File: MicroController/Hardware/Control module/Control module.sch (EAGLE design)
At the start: 53 parts, among them J1 1X2-3.5MM, J2 RJ45-TRAFO, J3 RJ45-TRAFO, J4 RJ45-TRAFO, Q1 BSS138, Q2 BSS138, Q3 BSS138, Q4 BSS138, Q5 BSS138, Q6 BSS138, Q7 BSS138, Q8 BSS138, U1 CD74HC4067SM96, U3 TLV1117-33CDCY

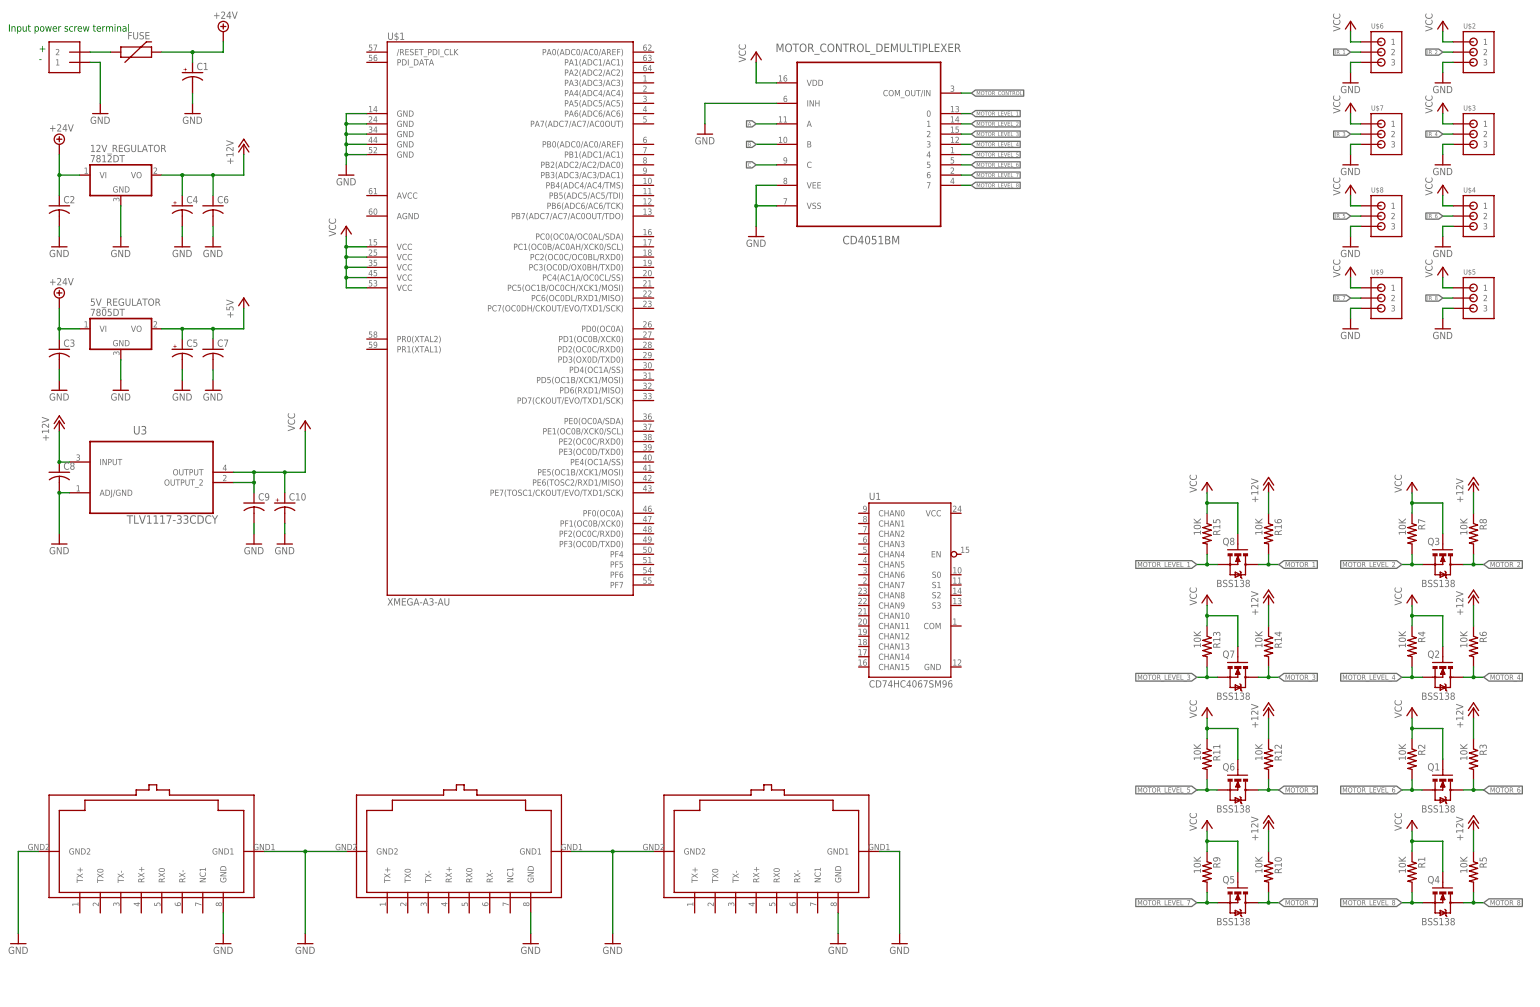
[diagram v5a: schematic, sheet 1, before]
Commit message: Looked into motor drivers and changed some components
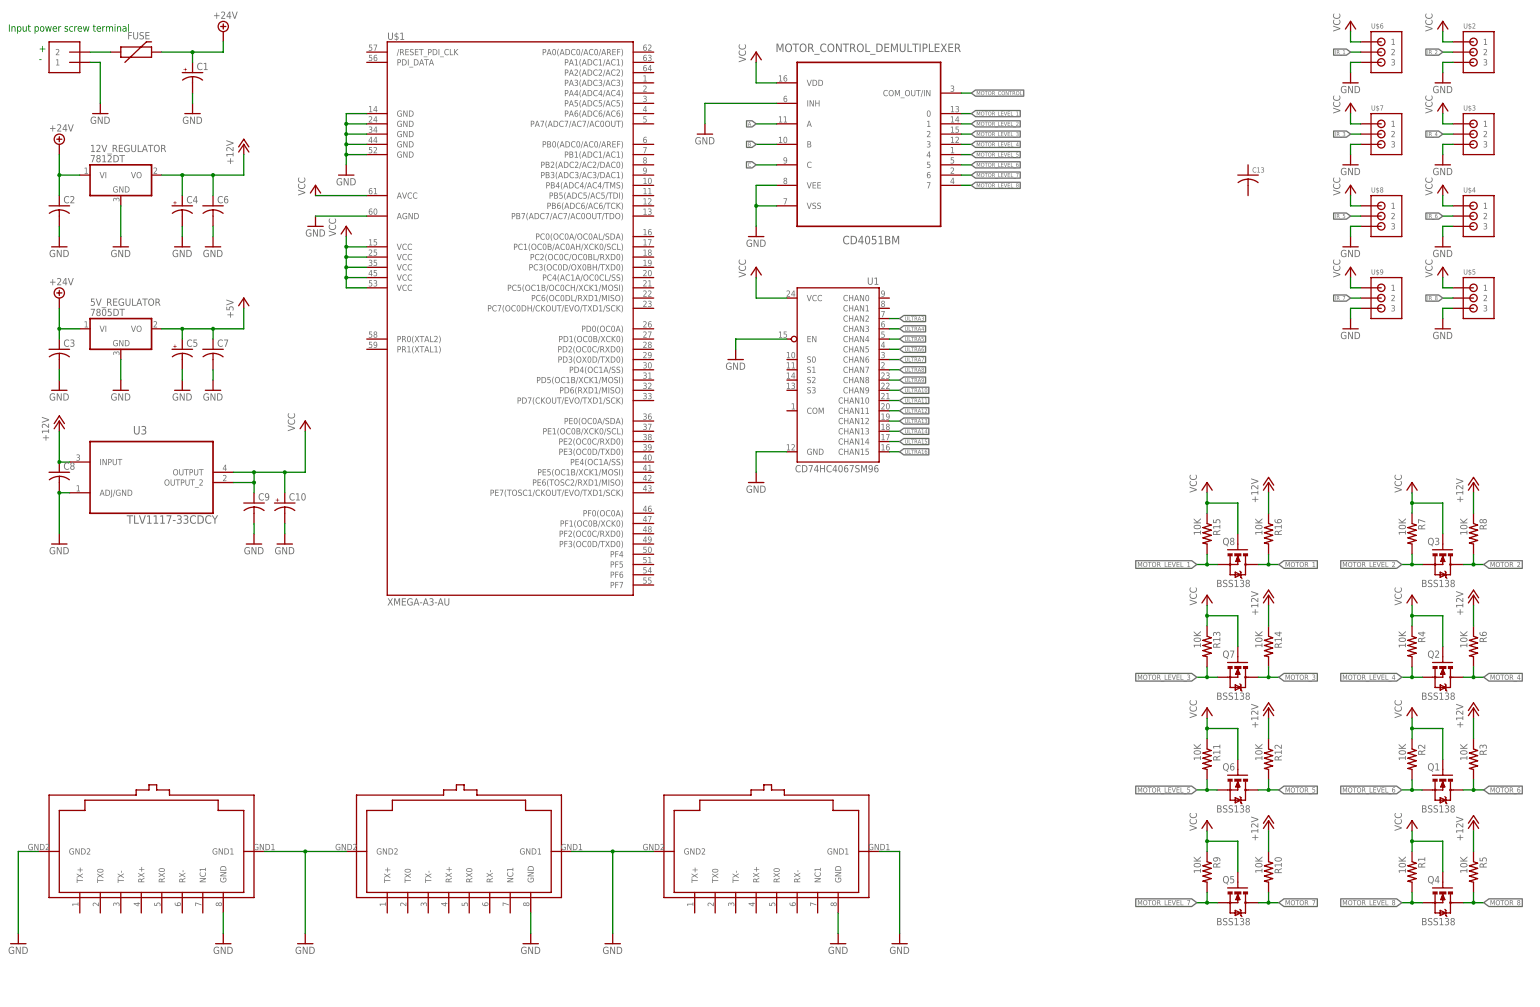
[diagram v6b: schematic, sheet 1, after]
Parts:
- added C13: (no value), adafruit:C-USC0805
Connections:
- new net ULTRA10: U1.CHAN9
- new net ULTRA11: U1.CHAN10
- new net ULTRA12: U1.CHAN11
- new net ULTRA13: U1.CHAN12
- new net ULTRA14: U1.CHAN13
- new net ULTRA15: U1.CHAN14
- new net ULTRA16: U1.CHAN15
- new net ULTRA3: U1.CHAN2
- new net ULTRA4: U1.CHAN3
- new net ULTRA5: U1.CHAN4
- new net ULTRA6: U1.CHAN5
- new net ULTRA7: U1.CHAN6
- new net ULTRA8: U1.CHAN7
- new net ULTRA9: U1.CHAN8
- net GND: now also U$1.AGND, U1.EN, U1.GND
- net VCC: now also U$1.AVCC, U1.VCC
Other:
- moved on the sheet: U1
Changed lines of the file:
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@@
 <part name="P+29" library="supply1" library_urn="urn:adsk.eagle:library:371" deviceset="VCC" device=""/>
 <part name="P+30" library="supply1" library_urn="urn:adsk.eagle:library:371" deviceset="VCC" device=""/>
+<part name="P+31" library="supply1" library_urn="urn:adsk.eagle:library:371" deviceset="VCC" device=""/>
+<part name="GND32" library="supply1" library_urn="urn:adsk.eagle:library:371" deviceset="GND" device=""/>
+<part name="GND33" library="supply1" library_urn="urn:adsk.eagle:library:371" deviceset="GND" device=""/>
+<part name="GND34" library="supply1" library_urn="urn:adsk.eagle:library:371" deviceset="GND" device=""/>
+<part name="P+32" library="supply1" library_urn="urn:adsk.eagle:library:371" deviceset="VCC" device=""/>
+<part name="C13" library="adafruit" library_urn="urn:adsk.eagle:library:420" deviceset="C-US" device="C0805"/>
 </parts>
 <sheets>
@@
 </plain>
 <instances>
-<instance part="U1" gate="U1" x="213.36" y="68.58"/>
+<instance part="U1" gate="U1" x="195.58" y="121.92" rot="MR0"/>
 <instance part="U$1" gate="G$1" x="114.3" y="134.62"/>
 <instance part="MOTOR_CONTROL_DEMULTIPLEXER" gate="A" x="203.2" y="180.34" smashed="yes">
@@
 <instance part="P+29" gate="VCC" x="345.44" y="147.32"/>
 <instance part="P+30" gate="VCC" x="322.58" y="147.32"/>
+<instance part="P+31" gate="VCC" x="66.04" y="167.64"/>
+<instance part="GND32" gate="1" x="66.04" y="157.48"/>
+<instance part="GND33" gate="1" x="175.26" y="93.98"/>
+<instance part="GND34" gate="1" x="170.18" y="124.46"/>
+<instance part="P+32" gate="VCC" x="175.26" y="147.32"/>
+<instance part="C13" gate="G$1" x="297.18" y="170.18" smashed="yes">
+<attribute name="NAME" x="298.196" y="170.815" size="1.27" layer="95"/>
+<attribute name="VALUE" x="298.196" y="165.989" size="1.778" layer="96"/>
+</instance>
 </instances>
 <busses>
@@
 <wire x1="322.58" y1="137.16" x2="322.58" y2="134.62" width="0.1524" layer="91"/>
 </segment>
+<segment>
+<pinref part="GND32" gate="1" pin="GND"/>
+<pinref part="U$1" gate="G$1" pin="AGND"/>
+<wire x1="66.04" y1="160.02" x2="78.74" y2="160.02" width="0.1524" layer="91"/>
+</segment>
+<segment>
+<pinref part="U1" gate="U1" pin="GND"/>
+<pinref part="GND33" gate="1" pin="GND"/>
+<wire x1="182.88" y1="101.6" x2="175.26" y2="101.6" width="0.1524" layer="91"/>
+<wire x1="175.26" y1="101.6" x2="175.26" y2="96.52" width="0.1524" layer="91"/>
+</segment>
+<segment>
+<pinref part="U1" gate="U1" pin="EN"/>
+<pinref part="GND34" gate="1" pin="GND"/>
+<wire x1="182.88" y1="129.54" x2="170.18" y2="129.54" width="0.1524" layer="91"/>
+<wire x1="170.18" y1="129.54" x2="170.18" y2="127" width="0.1524" layer="91"/>
+</segment>
 </net>
 <net name="VCC" class="0">
@@
 <wire x1="345.44" y1="142.24" x2="347.98" y2="142.24" width="0.1524" layer="91"/>
 </segment>
+<segment>
+<pinref part="P+31" gate="VCC" pin="VCC"/>
+<pinref part="U$1" gate="G$1" pin="AVCC"/>
+<wire x1="66.04" y1="165.1" x2="78.74" y2="165.1" width="0.1524" layer="91"/>
+</segment>
+<segment>
+<pinref part="P+32" gate="VCC" pin="VCC"/>
+<pinref part="U1" gate="U1" pin="VCC"/>
+<wire x1="175.26" y1="144.78" x2="175.26" y2="139.7" width="0.1524" layer="91"/>
+<wire x1="175.26" y1="139.7" x2="182.88" y2="139.7" width="0.1524" layer="91"/>
+</segment>
 </net>
 <net name="+12V" class="0">
@@
 </segment>
 </net>
+<net name="ULTRA3" class="0">
+<segment>
+<pinref part="U1" gate="U1" pin="CHAN2"/>
+<wire x1="208.28" y1="134.62" x2="210.82" y2="134.62" width="0.1524" layer="91"/>
+<label x="210.82" y="134.62" size="1.016" layer="95" xref="yes"/>
+</segment>
+</net>
+<net name="ULTRA4" class="0">
+<segment>
+<pinref part="U1" gate="U1" pin="CHAN3"/>
+<wire x1="208.28" y1="132.08" x2="210.82" y2="132.08" width="0.1524" layer="91"/>
+<label x="210.82" y="132.08" size="1.016" layer="95" xref="yes"/>
+</segment>
+</net>
+<net name="ULTRA5" class="0">
+<segment>
+<pinref part="U1" gate="U1" pin="CHAN4"/>
+<wire x1="208.28" y1="129.54" x2="210.82" y2="129.54" width="0.1524" layer="91"/>
+<label x="210.82" y="129.54" size="1.016" layer="95" xref="yes"/>
+</segment>
+</net>
+<net name="ULTRA6" class="0">
+<segment>
+<pinref part="U1" gate="U1" pin="CHAN5"/>
+<wire x1="208.28" y1="127" x2="210.82" y2="127" width="0.1524" layer="91"/>
+<label x="210.82" y="127" size="1.016" layer="95" xref="yes"/>
+</segment>
+</net>
+<net name="ULTRA7" class="0">
+<segment>
+<pinref part="U1" gate="U1" pin="CHAN6"/>
+<wire x1="208.28" y1="124.46" x2="210.82" y2="124.46" width="0.1524" layer="91"/>
+<label x="210.82" y="124.46" size="1.016" layer="95" xref="yes"/>
+</segment>
+</net>
+<net name="ULTRA8" class="0">
+<segment>
+<pinref part="U1" gate="U1" pin="CHAN7"/>
+<wire x1="208.28" y1="121.92" x2="210.82" y2="121.92" width="0.1524" layer="91"/>
+<label x="210.82" y="121.92" size="1.016" layer="95" xref="yes"/>
+</segment>
+</net>
+<net name="ULTRA9" class="0">
+<segment>
+<pinref part="U1" gate="U1" pin="CHAN8"/>
+<wire x1="208.28" y1="119.38" x2="210.82" y2="119.38" width="0.1524" layer="91"/>
+<label x="210.82" y="119.38" size="1.016" layer="95" xref="yes"/>
+</segment>
+</net>
+<net name="ULTRA10" class="0">
+<segment>
+<pinref part="U1" gate="U1" pin="CHAN9"/>
+<wire x1="208.28" y1="116.84" x2="210.82" y2="116.84" width="0.1524" layer="91"/>
+<label x="210.82" y="116.84" size="1.016" layer="95" xref="yes"/>
+</segment>
+</net>
+<net name="ULTRA11" class="0">
+<segment>
+<pinref part="U1" gate="U1" pin="CHAN10"/>
+<wire x1="208.28" y1="114.3" x2="210.82" y2="114.3" width="0.1524" layer="91"/>
+<label x="210.82" y="114.3" size="1.016" layer="95" xref="yes"/>
+</segment>
+</net>
+<net name="ULTRA12" class="0">
+<segment>
+<pinref part="U1" gate="U1" pin="CHAN11"/>
+<wire x1="208.28" y1="111.76" x2="210.82" y2="111.76" width="0.1524" layer="91"/>
+<label x="210.82" y="111.76" size="1.016" layer="95" xref="yes"/>
+</segment>
+</net>
+<net name="ULTRA13" class="0">
+<segment>
+<pinref part="U1" gate="U1" pin="CHAN12"/>
+<wire x1="208.28" y1="109.22" x2="210.82" y2="109.22" width="0.1524" layer="91"/>
+<label x="210.82" y="109.22" size="1.016" layer="95" xref="yes"/>
+</segment>
+</net>
+<net name="ULTRA14" class="0">
+<segment>
+<pinref part="U1" gate="U1" pin="CHAN13"/>
+<wire x1="208.28" y1="106.68" x2="210.82" y2="106.68" width="0.1524" layer="91"/>
+<label x="210.82" y="106.68" size="1.016" layer="95" xref="yes"/>
+</segment>
+</net>
+<net name="ULTRA15" class="0">
+<segment>
+<pinref part="U1" gate="U1" pin="CHAN14"/>
+<wire x1="208.28" y1="104.14" x2="210.82" y2="104.14" width="0.1524" layer="91"/>
+<label x="210.82" y="104.14" size="1.016" layer="95" xref="yes"/>
+</segment>
+</net>
+<net name="ULTRA16" class="0">
+<segment>
+<pinref part="U1" gate="U1" pin="CHAN15"/>
+<wire x1="208.28" y1="101.6" x2="210.82" y2="101.6" width="0.1524" layer="91"/>
+<label x="210.82" y="101.6" size="1.016" layer="95" xref="yes"/>
+</segment>
+</net>

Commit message: Connected several components, added RX TX connector
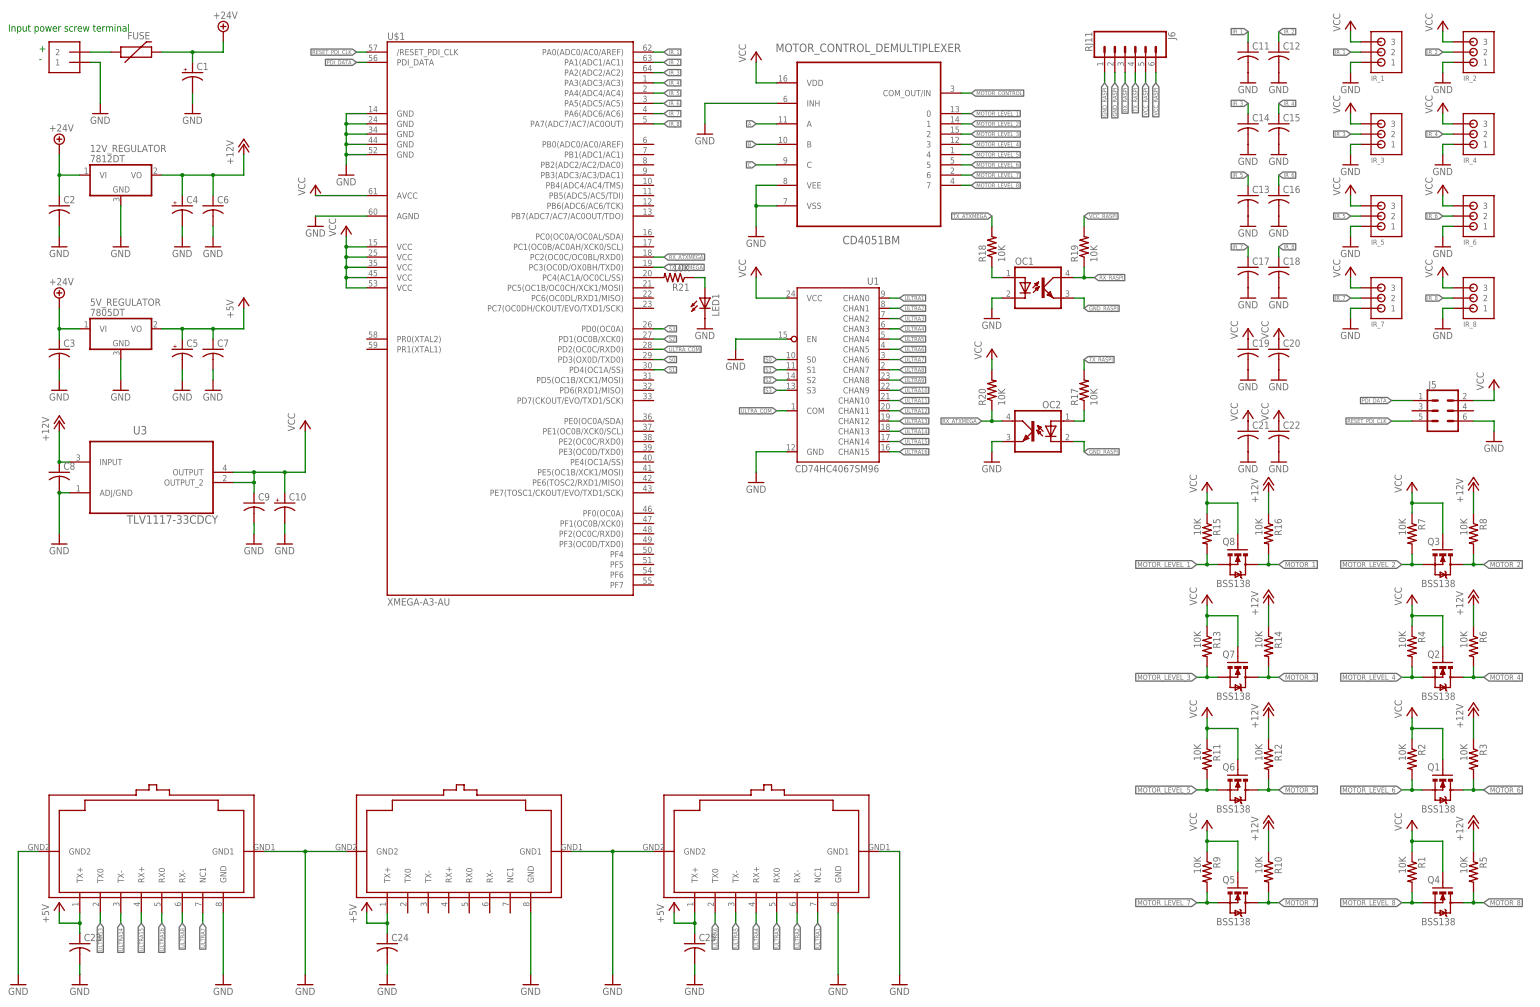
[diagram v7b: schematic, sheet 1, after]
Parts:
- added C11, C12, C14, C15, C16, C17, C18, C19, C20, C21, C22: (no value), adafruit:C-USC0603
- added C23, C24, C25: (no value), adafruit:C-USC0805
- added J5: (no value), SparkFun-Connectors:CONN_03X2SHROUD
- added J6: RJ11, SparkFun-Connectors:RJ11-6
- added LED1: (no value), led:LEDCHIPLED_0805
- added OC1, OC2: (no value), optocoupler:PC817
- added R17, R18, R19, R20, R21: 10K, adafruit:R-US_R0805
- C13: device adafruit:C-USC0805 -> adafruit:C-USC0603
- renumbered U$2 to IR_2, U$3 to IR_4, U$4 to IR_6, U$5 to IR_8, U$6 to IR_1, U$7 to IR_3, U$8 to IR_5, U$9 to IR_7
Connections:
- new net GND_RASPI: J6.1, J6.2, OC1.EMIT, OC2.C
- new net N$1: OC1.A, R18.1
- new net N$2: OC2.A, R17.1
- new net N$3: R21.2, U$1.PC4(AC1A/OC0CL/SS)
- new net N$4: LED1.A, R21.1
- new net PDI_DATA: J5.1, U$1.PDI_DATA
- new net RESET_PDI_CLK: J5.5, U$1./RESET_PDI_CLK
- new net RX_ATXMEGA: OC2.COL, R20.1, U$1.PC2(OC0C/OC0BL/RXD0)
- new net RX_RASPI: J6.3, OC1.COL, R19.1
- new net S0: U$1.PD3(OX0D/TXD0), U1.S0
- new net S1: U$1.PD4(OC1A/SS), U1.S1
- new net S2: U$1.PD1(OC0B/XCK0), U1.S2
- new net S3: U$1.PD0(OC0A), U1.S3
- new net TX_ATXMEGA: R18.2, U$1.PC3(OC0D/OX0BH/TXD0)
- new net TX_RASPI: J6.4, R17.2
- new net ULTRA1: J2.NC1, U1.CHAN0
- new net ULTRA2: J2.RX-, U1.CHAN1
- new net ULTRA_COM: U$1.PD2(OC0C/RXD0), U1.COM
- new net VCC_RASPI: J6.5, J6.6, R19.2
- net +5V: now also C23.1, C24.1, C25.1, J2.TX+, J3.TX+, J4.TX+
- net GND: now also C11.2, C12.2, C13.2, C14.2, C15.2, C16.2, C17.2, C18.2, C19.2, C20.2, C21.2, C22.2, C23.2, C24.2, C25.2, IR_1.1, IR_2.1, IR_3.1, IR_4.1, IR_5.1, IR_6.1, IR_7.1, IR_8.1, J5.6, LED1.C, OC1.C, OC2.EMIT; no longer IR_1.3, IR_2.3, IR_3.3, IR_4.3, IR_5.3, IR_6.3, IR_7.3, IR_8.3
- net IR_1: now also C11.1, U$1.PA0(ADC0/AC0/AREF)
- net IR_2: now also C12.1, U$1.PA1(ADC1/AC1)
- net IR_3: now also C14.1, U$1.PA2(ADC2/AC2)
- net IR_4: now also C15.1, U$1.PA3(ADC3/AC3)
- net IR_5: now also C13.1, U$1.PA4(ADC4/AC4)
- net IR_6: now also C16.1, U$1.PA5(ADC5/AC5)
- net IR_7: now also C17.1, U$1.PA6(ADC6/AC6)
- net IR_8: now also C18.1, U$1.PA7(ADC7/AC7/AC0OUT)
- net ULTRA13: now also J3.TX0
- net ULTRA14: now also J3.TX-
- net ULTRA15: now also J3.RX+
- net ULTRA16: now also J3.RX0
- net ULTRA3: now also J2.RX0
- net ULTRA4: now also J2.RX+
- net ULTRA5: now also J2.TX-
- net ULTRA6: now also J2.TX0
- net ULTRA7: now also J3.NC1
- net ULTRA8: now also J3.RX-
- net VCC: now also C19.1, C20.1, C21.1, C22.1, IR_1.3, IR_2.3, IR_3.3, IR_4.3, IR_5.3, IR_6.3, IR_7.3, IR_8.3, J5.2, R20.2; no longer IR_1.1, IR_2.1, IR_3.1, IR_4.1, IR_5.1, IR_6.1, IR_7.1, IR_8.1
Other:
- moved on the sheet: C13
